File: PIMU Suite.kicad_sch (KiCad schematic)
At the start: 4 parts, among them J1 Conn_01x05, U1 Teensy4.1, U2 MICROSD_SPI_OR_SDIO_CARD

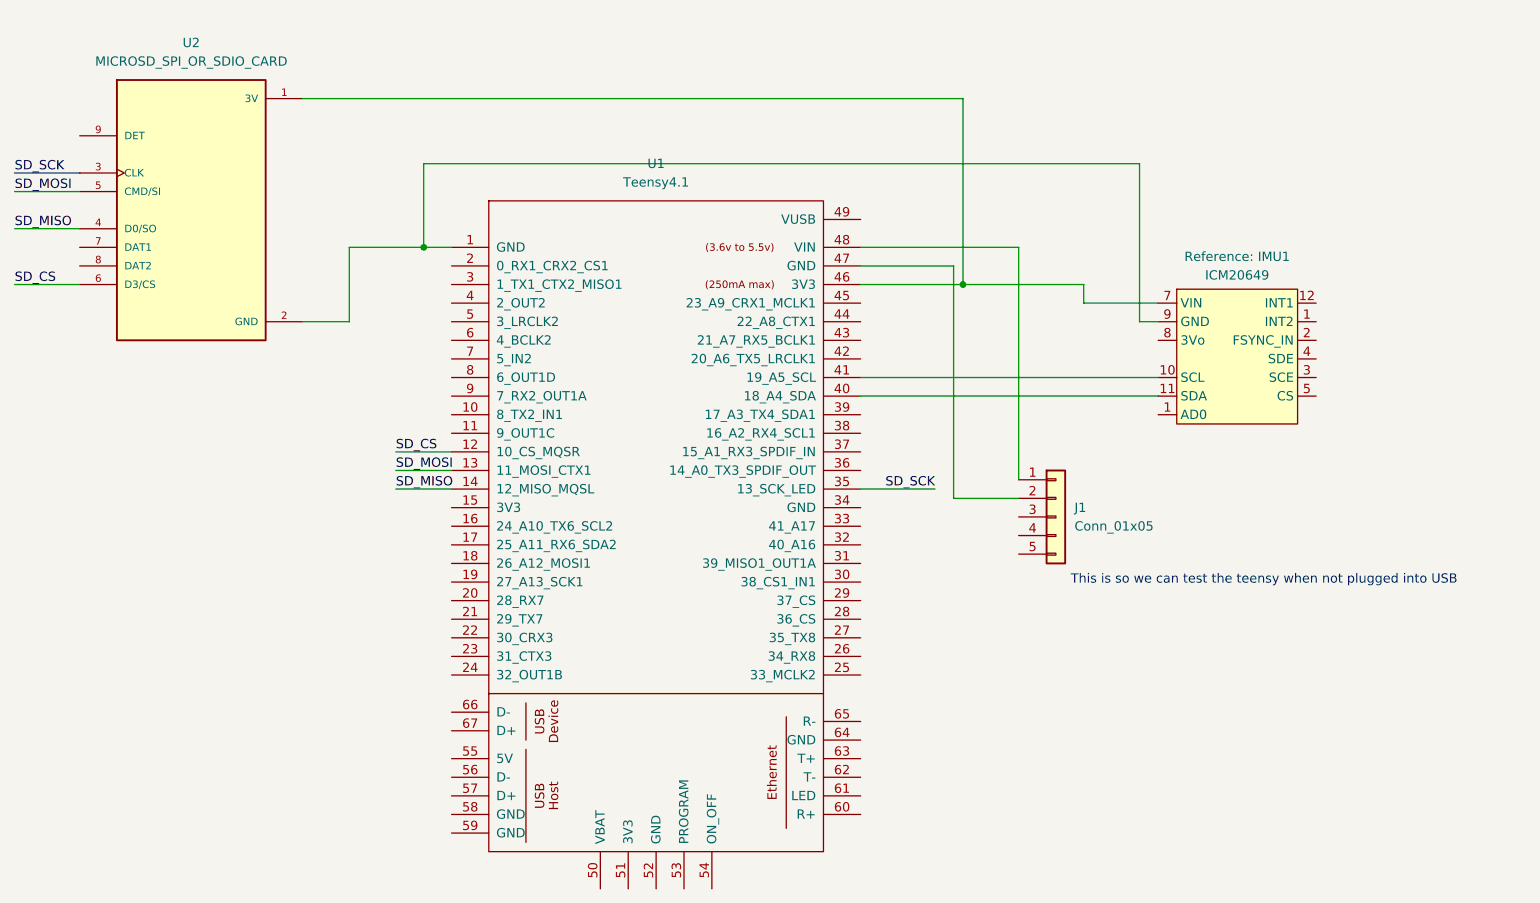
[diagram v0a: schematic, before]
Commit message: added pressure
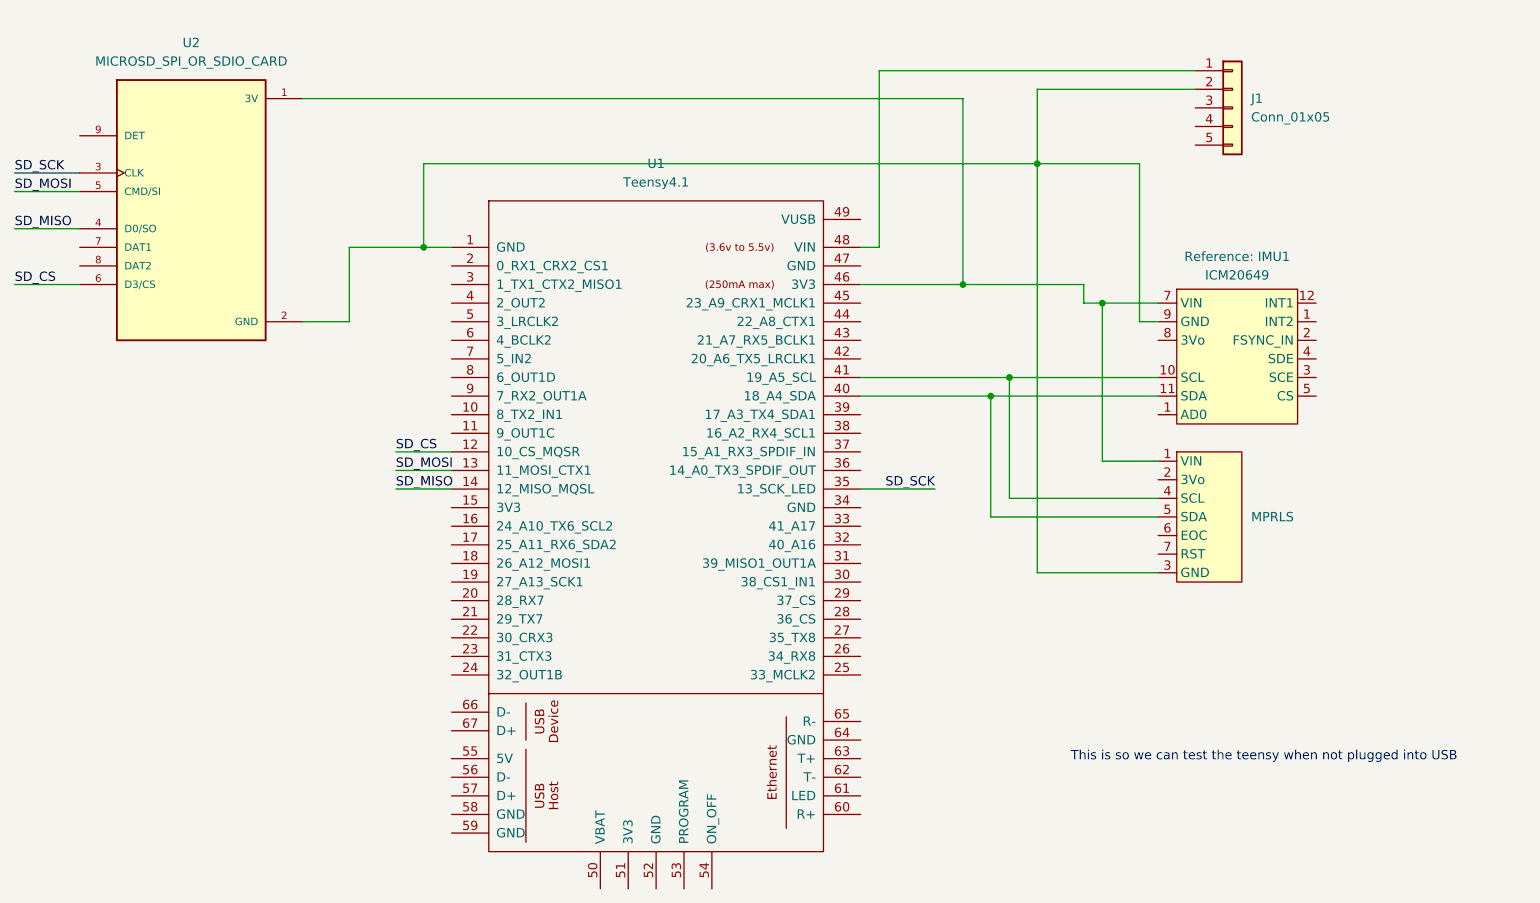
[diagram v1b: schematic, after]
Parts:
- added PRESSURE1: MPRLS, RSX:MPRLS_Pressure, symbol RSX:MPRLS_Pressure
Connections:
- net at IMU1.10 (SCL), U1.41 (19_A5_SCL): now also PRESSURE1.4 (SCL)
- net at IMU1.11 (SDA), U1.40 (18_A4_SDA): now also PRESSURE1.5 (SDA)
- net at IMU1.7 (VIN), U1.46 (3V3), U2.1 (3V): now also PRESSURE1.1 (VIN)
- net at IMU1.9 (GND), U1.1 (GND), U2.2 (GND): now also J1.2 (Pin_2), PRESSURE1.3 (GND)
- net at U1.47 (GND): no longer J1.2 (Pin_2)
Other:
- moved on the sheet: J1
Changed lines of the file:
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@@
 	(text "This is so we can test the teensy when not plugged into USB"
 		(exclude_from_sim no)
-		(at 227.838 105.156 0)
+		(at 227.838 129.286 0)
 		(effects
 			(font
@@
 			)
 		)
+	)
+	(junction
+		(at 205.74 67.31)
+		(diameter 0)
+		(color 0 0 0 0)
 	)
 	(junction
@@
 		(color 0 0 0 0)
 	)
+	(junction
+		(at 193.04 77.47)
+		(diameter 0)
+		(color 0 0 0 0)
+	)
+	(junction
+		(at 190.5 80.01)
+		(diameter 0)
+		(color 0 0 0 0)
+	)
+	(junction
+		(at 196.85 48.26)
+		(diameter 0)
+		(color 0 0 0 0)
+	)
+	(wire
+		(pts
+			(xy 213.36 104.14) (xy 196.85 104.14)
+		)
+		(stroke
+			(width 0)
+			(type default)
+		)
+	)
 	(wire
 		(pts
@@
 	(wire
 		(pts
+			(xy 190.5 96.52) (xy 213.36 96.52)
+		)
+		(stroke
+			(width 0)
+			(type default)
+		)
+	)
+	(wire
+		(pts
+			(xy 196.85 104.14) (xy 196.85 48.26)
+		)
+		(stroke
+			(width 0)
+			(type default)
+		)
+	)
+	(wire
+		(pts
 			(xy 102.87 69.85) (xy 102.87 59.69)
 		)
@@
 	(wire
 		(pts
+			(xy 218.44 35.56) (xy 175.26 35.56)
+		)
+		(stroke
+			(width 0)
+			(type default)
+		)
+	)
+	(wire
+		(pts
 			(xy 109.22 92.71) (xy 116.84 92.71)
 		)
@@
 	(wire
 		(pts
+			(xy 196.85 38.1) (xy 196.85 48.26)
+		)
+		(stroke
+			(width 0)
+			(type default)
+		)
+	)
+	(wire
+		(pts
 			(xy 186.69 64.77) (xy 186.69 39.37)
 		)
@@
 	(wire
 		(pts
-			(xy 194.31 93.98) (xy 185.42 93.98)
-		)
-		(stroke
-			(width 0)
-			(type default)
-		)
-	)
-	(wire
-		(pts
-			(xy 213.36 67.31) (xy 203.2 67.31)
+			(xy 213.36 67.31) (xy 205.74 67.31)
 		)
 		(stroke
@@
 	(wire
 		(pts
-			(xy 185.42 93.98) (xy 185.42 62.23)
+			(xy 193.04 77.47) (xy 213.36 77.47)
 		)
 		(stroke
@@
 	(wire
 		(pts
+			(xy 175.26 35.56) (xy 175.26 59.69)
+		)
+		(stroke
+			(width 0)
+			(type default)
+		)
+	)
+	(wire
+		(pts
+			(xy 218.44 38.1) (xy 196.85 38.1)
+		)
+		(stroke
+			(width 0)
+			(type default)
+		)
+	)
+	(wire
+		(pts
 			(xy 102.87 59.69) (xy 113.03 59.69)
 		)
@@
 	(wire
 		(pts
-			(xy 172.72 77.47) (xy 213.36 77.47)
+			(xy 205.74 88.9) (xy 205.74 67.31)
+		)
+		(stroke
+			(width 0)
+			(type default)
+		)
+	)
+	(wire
+		(pts
+			(xy 175.26 59.69) (xy 172.72 59.69)
 		)
 		(stroke
@@
 	(wire
 		(pts
-			(xy 194.31 59.69) (xy 172.72 59.69)
-		)
-		(stroke
-			(width 0)
-			(type default)
-		)
-	)
-	(wire
-		(pts
 			(xy 172.72 64.77) (xy 186.69 64.77)
 		)
@@
 		)
 	)
-	(wire
-		(pts
-			(xy 172.72 80.01) (xy 213.36 80.01)
-		)
-		(stroke
-			(width 0)
-			(type default)
-		)
-	)
 	(bus
 		(pts
@@
 	(wire
 		(pts
-			(xy 194.31 91.44) (xy 194.31 59.69)
+			(xy 172.72 80.01) (xy 190.5 80.01)
+		)
+		(stroke
+			(width 0)
+			(type default)
+		)
+	)
+	(wire
+		(pts
+			(xy 172.72 77.47) (xy 193.04 77.47)
+		)
+		(stroke
+			(width 0)
+			(type default)
+		)
+	)
+	(wire
+		(pts
+			(xy 196.85 48.26) (xy 113.03 48.26)
 		)
 		(stroke
@@
 	(wire
 		(pts
-			(xy 185.42 62.23) (xy 172.72 62.23)
-		)
-		(stroke
-			(width 0)
-			(type default)
-		)
-	)
-	(wire
-		(pts
 			(xy 109.22 90.17) (xy 116.84 90.17)
 		)
@@
 	(wire
 		(pts
+			(xy 193.04 93.98) (xy 193.04 77.47)
+		)
+		(stroke
+			(width 0)
+			(type default)
+		)
+	)
+	(wire
+		(pts
 			(xy 57.15 57.15) (xy 66.04 57.15)
 		)
@@
 	(wire
 		(pts
-			(xy 210.82 48.26) (xy 113.03 48.26)
+			(xy 210.82 48.26) (xy 196.85 48.26)
+		)
+		(stroke
+			(width 0)
+			(type default)
+		)
+	)
+	(wire
+		(pts
+			(xy 213.36 88.9) (xy 205.74 88.9)
 		)
 		(stroke
@@
 	(wire
 		(pts
+			(xy 205.74 67.31) (xy 203.2 67.31)
+		)
+		(stroke
+			(width 0)
+			(type default)
+		)
+	)
+	(wire
+		(pts
+			(xy 190.5 96.52) (xy 190.5 80.01)
+		)
+		(stroke
+			(width 0)
+			(type default)
+		)
+	)
+	(wire
+		(pts
+			(xy 193.04 93.98) (xy 213.36 93.98)
+		)
+		(stroke
+			(width 0)
+			(type default)
+		)
+	)
+	(wire
+		(pts
 			(xy 57.15 64.77) (xy 66.04 64.77)
+		)
+		(stroke
+			(width 0)
+			(type default)
+		)
+	)
+	(wire
+		(pts
+			(xy 190.5 80.01) (xy 213.36 80.01)
 		)
 		(stroke
@@
 			)
 			(justify right bottom)
+		)
+	)
+	(symbol
+		(lib_id "RSX:MPRLS_Pressure")
+		(at 219.71 96.52 0)
+		(unit 1)
+		(exclude_from_sim no)
+		(in_bom yes)
+		(on_board yes)
+		(dnp no)
+		(fields_autoplaced yes)
+		(property "Reference" "PRESSURE1"
+			(at 220.218 83.82 0)
+			(effects
+				(font
+					(size 1.27 1.27)
+				)
+				(hide yes)
+			)
+		)
+		(property "Value" "MPRLS"
+			(at 226.06 96.5199 0)
+			(effects
+				(font
+					(size 1.27 1.27)
+				)
+				(justify left)
+			)
+		)
+		(property "Footprint" "RSX:MPRLS_Pressure"
+			(at 219.71 96.52 0)
+			(effects
+				(font
+					(size 1.27 1.27)
+				)
+				(hide yes)
+			)
+		)
+		(property "Datasheet" ""
+			(at 219.71 96.52 0)
+			(effects
+				(font
+					(size 1.27 1.27)
+				)
+				(hide yes)
+			)
+		)
+		(property "Description" ""
+			(at 219.71 96.52 0)
+			(effects
+				(font
+					(size 1.27 1.27)
+				)
+				(hide yes)
+			)
+		)
+		(pin "5"
+		)
+		(pin "6"
+		)
+		(pin "3"
+		)
+		(pin "1"
+		)
+		(pin "4"
+		)
+		(pin "7"
+		)
+		(pin "2"
+		)
+		(instances
+			(project ""
+				(path "/f92a9e59-93af-435a-9a9e-44bda57be41a"
+					(reference "PRESSURE1")
+					(unit 1)
+				)
+			)
 		)
 	)
@@
 	(symbol
 		(lib_id "Connector_Generic:Conn_01x05")
-		(at 199.39 96.52 0)
+		(at 223.52 40.64 0)
 		(unit 1)
 		(exclude_from_sim no)
@@
 		(fields_autoplaced yes)
 		(property "Reference" "J1"
-			(at 201.93 95.2499 0)
+			(at 226.06 39.3699 0)
 			(effects
 				(font
@@
 		)
 		(property "Value" "Conn_01x05"
-			(at 201.93 97.7899 0)
+			(at 226.06 41.9099 0)
 			(effects
 				(font
@@
 		)
 		(property "Footprint" "Connector_PinHeader_1.00mm:PinHeader_1x05_P1.00mm_Vertical"
-			(at 199.39 96.52 0)
+			(at 223.52 40.64 0)
 			(effects
 				(font
@@
 		)
 		(property "Datasheet" "~"
-			(at 199.39 96.52 0)
+			(at 223.52 40.64 0)
 			(effects
 				(font
@@
 		)
 		(property "Description" "Generic connector, single row, 01x05, script generated (kicad-library-utils/schlib/autogen/connector/)"
-			(at 199.39 96.52 0)
-			(effects
-				(font
+			(at 223.52 40.64 0)
+			(effects
+				(font

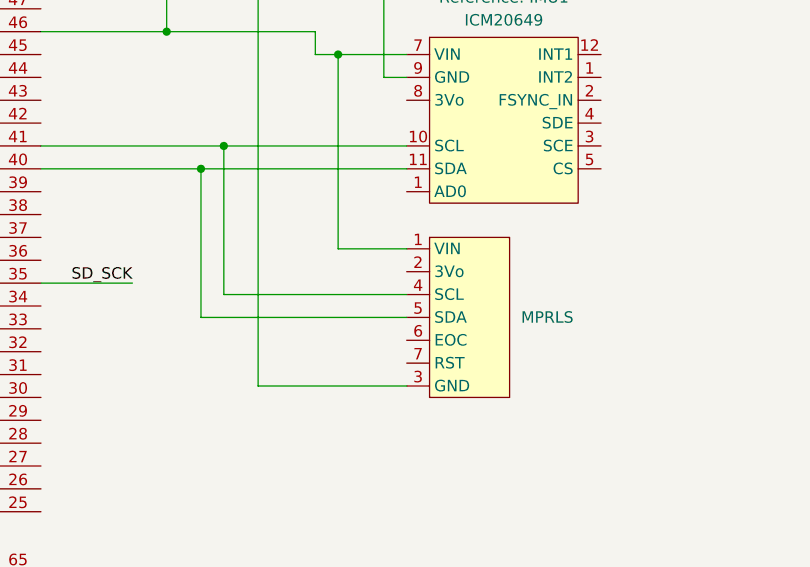
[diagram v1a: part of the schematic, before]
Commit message: Using new pressure sensor
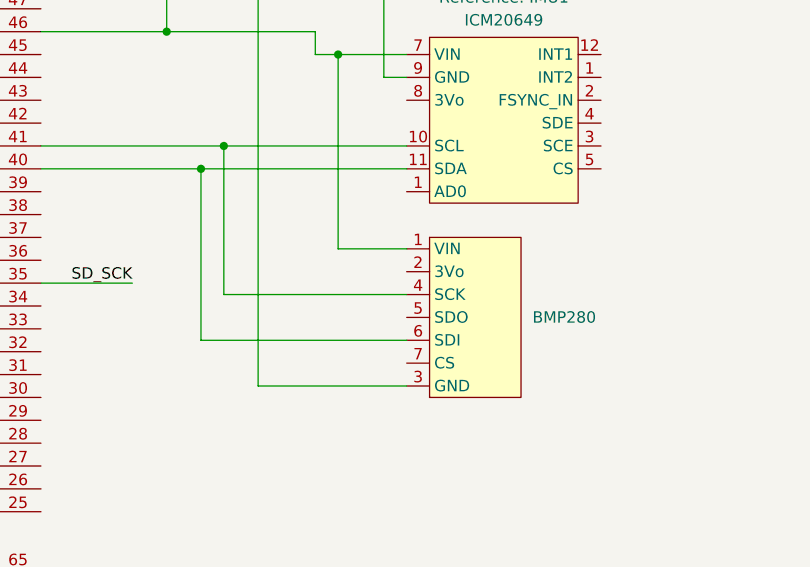
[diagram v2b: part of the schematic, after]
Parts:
- removed PRESSURE1: MPRLS, RSX:MPRLS_Pressure, symbol RSX:MPRLS_Pressure
- added BMP1: BMP280, RSX:BMP280, symbol RSX:BMP280
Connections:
- net at IMU1.7 (VIN), U1.46 (3V3), U2.1 (3V): now also BMP1.1 (VIN)
- net at IMU1.9 (GND), J1.2 (Pin_2), U1.1 (GND)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: now also BMP1.3 (GND)
- net at IMU1.10 (SCL), U1.41 (19_A5_SCL): now also BMP1.4 (SCK)
- net at IMU1.11 (SDA), U1.40 (18_A4_SDA): now also BMP1.6 (SDI)
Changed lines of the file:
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@@
-	(wire
-		(pts
-			(xy 190.5 96.52) (xy 213.36 96.52)
-		)
-		(stroke
-			(width 0)
-			(type default)
-		)
-	)
 	(wire
 		(pts
@@
 	(wire
 		(pts
+			(xy 190.5 99.06) (xy 213.36 99.06)
+		)
+		(stroke
+			(width 0)
+			(type default)
+		)
+	)
+	(wire
+		(pts
 			(xy 113.03 48.26) (xy 113.03 59.69)
 		)
@@
 	(wire
 		(pts
-			(xy 190.5 96.52) (xy 190.5 80.01)
+			(xy 190.5 80.01) (xy 190.5 99.06)
 		)
 		(stroke
@@
 			)
 			(justify right bottom)
-		)
-	)
-	(symbol
-		(lib_id "RSX:MPRLS_Pressure")
-		(at 219.71 96.52 0)
-		(unit 1)
-		(exclude_from_sim no)
-		(in_bom yes)
-		(on_board yes)
-		(dnp no)
-		(fields_autoplaced yes)
-		(property "Reference" "PRESSURE1"
-			(at 220.218 83.82 0)
-			(effects
-				(font
-					(size 1.27 1.27)
-				)
-				(hide yes)
-			)
-		)
-		(property "Value" "MPRLS"
-			(at 226.06 96.5199 0)
-			(effects
-				(font
-					(size 1.27 1.27)
-				)
-				(justify left)
-			)
-		)
-		(property "Footprint" "RSX:MPRLS_Pressure"
-			(at 219.71 96.52 0)
-			(effects
-				(font
-					(size 1.27 1.27)
-				)
-				(hide yes)
-			)
-		)
-		(property "Datasheet" ""
-			(at 219.71 96.52 0)
-			(effects
-				(font
-					(size 1.27 1.27)
-				)
-				(hide yes)
-			)
-		)
-		(property "Description" ""
-			(at 219.71 96.52 0)
-			(effects
-				(font
-					(size 1.27 1.27)
-				)
-				(hide yes)
-			)
-		)
-		(pin "5"
-		)
-		(pin "6"
-		)
-		(pin "3"
-		)
-		(pin "1"
-		)
-		(pin "4"
-		)
-		(pin "7"
-		)
-		(pin "2"
-		)
-		(instances
-			(project ""
-				(path "/f92a9e59-93af-435a-9a9e-44bda57be41a"
-					(reference "PRESSURE1")
-					(unit 1)
-				)
-			)
 		)
 	)
@@
 					(unit 1)
 				)
+			)
+		)
+	)
+	(symbol
+		(lib_id "RSX:BMP280")
+		(at 220.98 92.71 0)
+		(unit 1)
+		(exclude_from_sim no)
+		(in_bom yes)
+		(on_board yes)
+		(dnp no)
+		(fields_autoplaced yes)
+		(property "Reference" "BMP1"
+			(at 220.98 83.82 0)
+			(effects
+				(font
+					(size 1.27 1.27)
+				)
+				(hide yes)
+			)
+		)
+		(property "Value" "BMP280"
+			(at 227.33 96.5199 0)
+			(effects
+				(font
+					(size 1.27 1.27)
+				)
+				(justify left)
+			)
+		)
+		(property "Footprint" "RSX:BMP280"
+			(at 220.98 92.71 0)
+			(effects
+				(font
+					(size 1.27 1.27)
+				)
+				(hide yes)
+			)
+		)
+		(property "Datasheet" ""
+			(at 220.98 92.71 0)
+			(effects
+				(font
+					(size 1.27 1.27)
+				)
+				(hide yes)
+			)
+		)
+		(property "Description" ""
+			(at 220.98 92.71 0)
+			(effects
+				(font
+					(size 1.27 1.27)
+				)
+				(hide yes)
+			)
+		)
+		(pin "2"
+		)
+		(pin "3"
+		)
+		(pin "4"
+		)
+		(pin "5"
+		)
+		(pin "6"
+		)
+		(pin "1"
+		)
+		(pin "7"
+		)
+		(instances
+			(project ""
+				(path "/f92a9e59-93af-435a-9a9e-44bda57be41a"
+					(reference "BMP1")
+					(unit 1)
+				)
